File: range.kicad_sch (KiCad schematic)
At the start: 0 parts

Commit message: updated poer and range sensor scheamtics
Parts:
- added J2, J3, J4, J5, J6: Screw_Terminal_01x04, Connector_Dsub:DSUB-37_Pins_EdgeMount_P2.77mm, symbol Connector:Screw_Terminal_01x04
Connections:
- new net +3.3V: J2.1 (Pin_1), J3.1 (Pin_1), J4.1 (Pin_1), J5.1 (Pin_1), J6.1 (Pin_1)
- new net GND: J2.4 (Pin_4), J3.4 (Pin_4), J4.4 (Pin_4), J5.4 (Pin_4), J6.4 (Pin_4)
- new net SCL: J2.2 (Pin_2), J3.2 (Pin_2), J4.2 (Pin_2), J5.2 (Pin_2), J6.2 (Pin_2)
- new net SDA: J2.3 (Pin_3), J3.3 (Pin_3), J4.3 (Pin_3), J5.3 (Pin_3), J6.3 (Pin_3)
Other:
- note added: "Range Sensor Front"
- note added: "Range Sensor Front Left"
- note added: "Range Sensor Front Right"
- note added: "Range Sensor Left"
- note added: "Range Sensor Right"

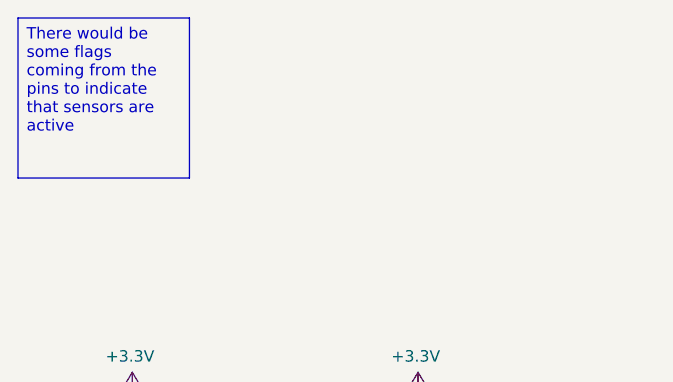
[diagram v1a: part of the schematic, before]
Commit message: added I2C lines
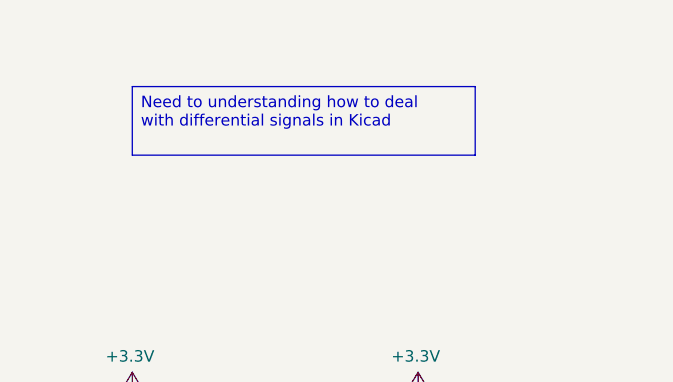
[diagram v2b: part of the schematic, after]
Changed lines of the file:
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@@
 		)
 	)
-	(text_box "There would be some flags coming from the pins to indicate that sensors are active "
+	(text_box "Need to understanding how to deal with differential signals in Kicad "
 		(exclude_from_sim no)
-		(at 20.32 16.51 0)
-		(size 19.05 17.78)
+		(at 33.02 24.13 0)
+		(size 38.1 7.62)
 		(margins 0.9525 0.9525 0.9525 0.9525)
 		(stroke

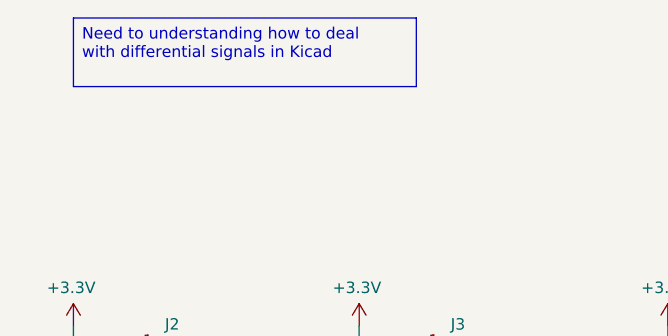
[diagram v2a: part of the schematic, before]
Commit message: added IR receiver circuit
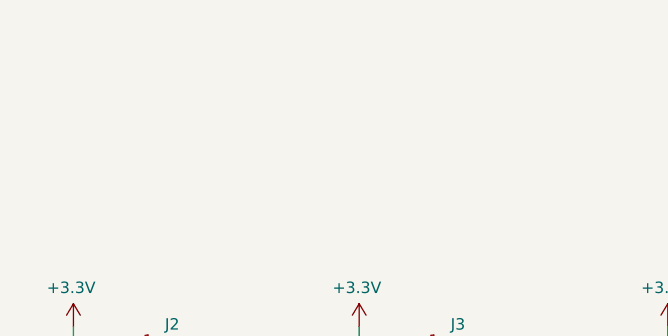
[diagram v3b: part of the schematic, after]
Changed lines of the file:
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@@
-		)
-	)
-	(text_box "Need to understanding how to deal with differential signals in Kicad "
-		(exclude_from_sim no)
-		(at 33.02 24.13 0)
-		(size 38.1 7.62)
-		(margins 0.9525 0.9525 0.9525 0.9525)
-		(stroke
-			(width 0)
-			(type solid)
-		)
-		(fill
-			(type none)
-		)
-		(effects
-			(font
-				(size 1.27 1.27)
-			)
-			(justify left top)
 		)
 	)

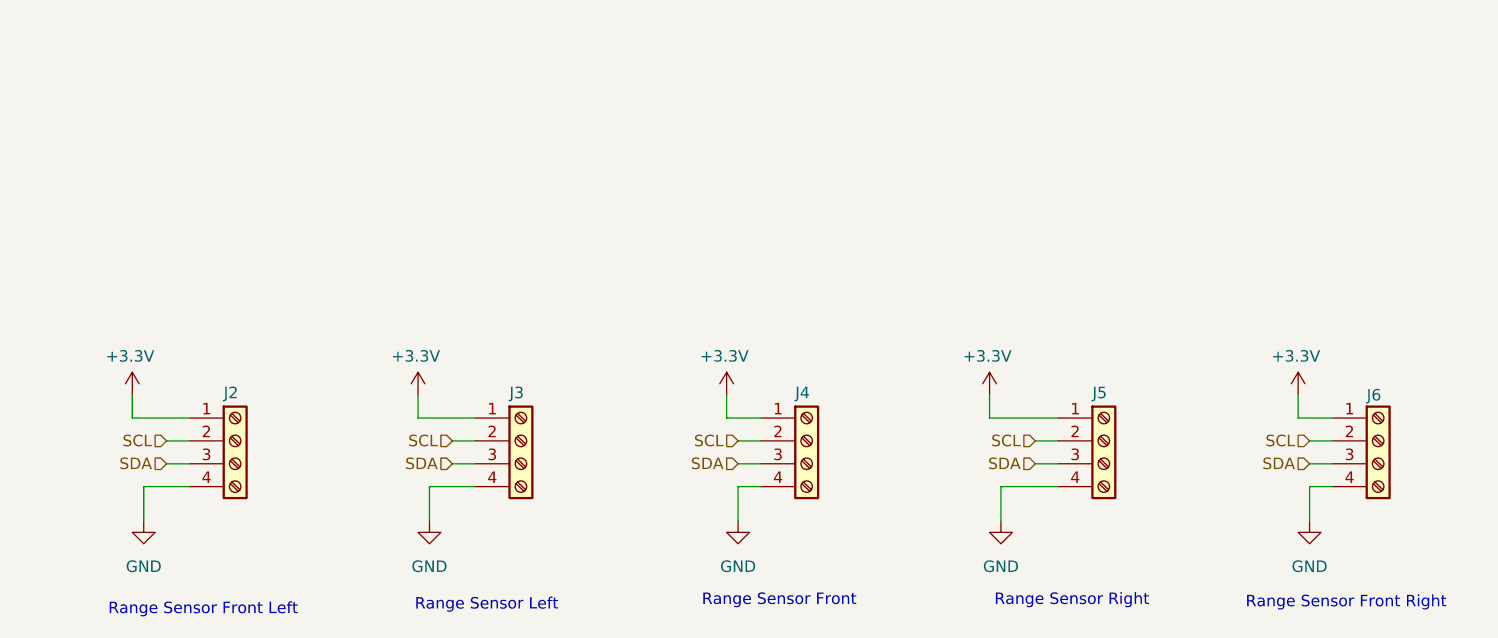
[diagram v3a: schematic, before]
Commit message: started adding DC Motor controller logic
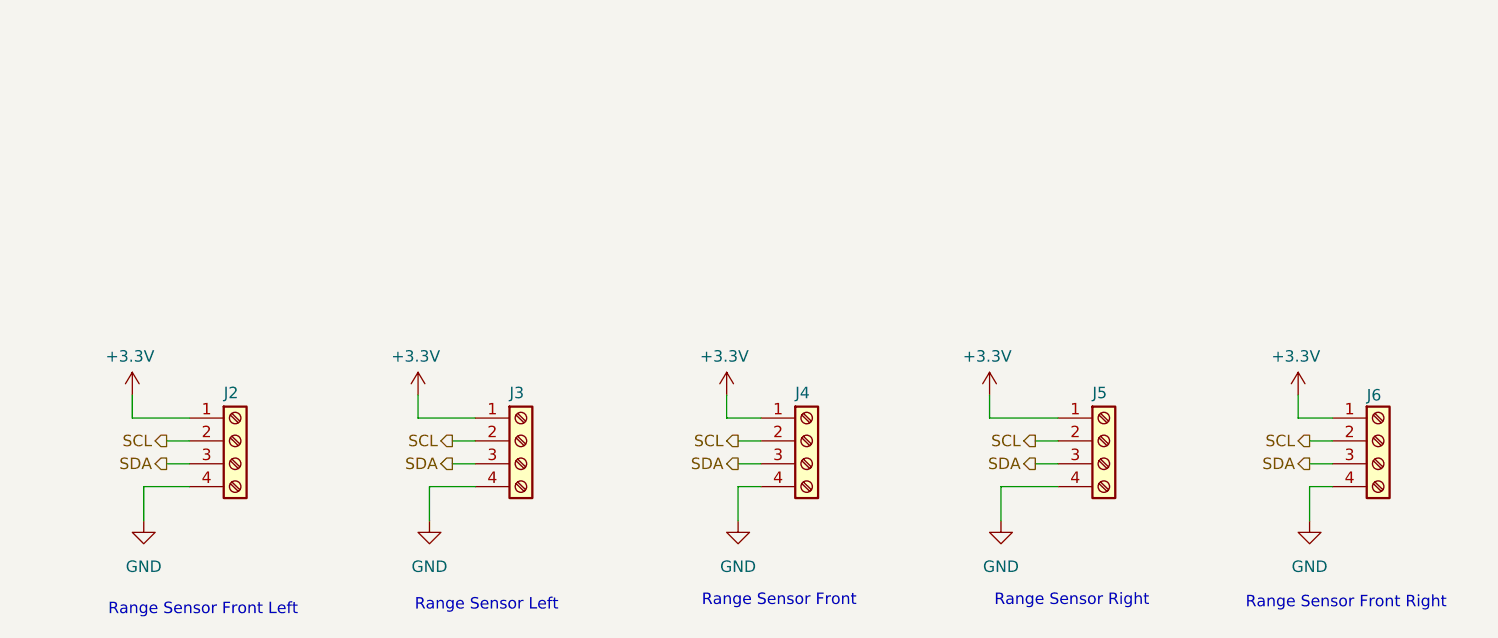
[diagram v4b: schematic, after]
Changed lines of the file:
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@@
 	)
 	(hierarchical_label "SDA"
-		(shape input)
+		(shape output)
 		(at 133.35 66.04 180)
 		(effects
@@
 	)
 	(hierarchical_label "SDA"
-		(shape input)
+		(shape output)
 		(at 68.58 66.04 180)
 		(effects
@@
 	)
 	(hierarchical_label "SDA"
-		(shape input)
+		(shape output)
 		(at 100.33 66.04 180)
 		(effects
@@
 	)
 	(hierarchical_label "SCL"
-		(shape input)
+		(shape output)
 		(at 133.35 63.5 180)
 		(effects
@@
 	)
 	(hierarchical_label "SCL"
-		(shape input)
+		(shape output)
 		(at 36.83 63.5 180)
 		(effects
@@
 	)
 	(hierarchical_label "SDA"
-		(shape input)
+		(shape output)
 		(at 163.83 66.04 180)
 		(effects
@@
 	)
 	(hierarchical_label "SCL"
-		(shape input)
+		(shape output)
 		(at 68.58 63.5 180)
 		(effects
@@
 	)
 	(hierarchical_label "SCL"
-		(shape input)
+		(shape output)
 		(at 100.33 63.5 180)
 		(effects
@@
 	)
 	(hierarchical_label "SDA"
-		(shape input)
+		(shape output)
 		(at 36.83 66.04 180)
 		(effects
@@
 	)
 	(hierarchical_label "SCL"
-		(shape input)
+		(shape output)
 		(at 163.83 63.5 180)
 		(effects

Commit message: started layout of Rev A
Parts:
- J2, J3, J4, J5, J6: footprint Connector_Dsub:DSUB-37_Pins_EdgeMount_P2.77mm -> TerminalBlock:TerminalBlock_Altech_AK300-4_P5.00mm
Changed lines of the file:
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@@
 			)
 		)
-		(property "Footprint" "Connector_Dsub:DSUB-37_Pins_EdgeMount_P2.77mm"
+		(property "Footprint" "TerminalBlock:TerminalBlock_Altech_AK300-4_P5.00mm"
 			(at 76.2 63.5 0)
 			(effects
@@
 			)
 		)
-		(property "Footprint" "Connector_Dsub:DSUB-37_Pins_EdgeMount_P2.77mm"
+		(property "Footprint" "TerminalBlock:TerminalBlock_Altech_AK300-4_P5.00mm"
 			(at 171.45 63.5 0)
 			(effects
@@
 			)
 		)
-		(property "Footprint" "Connector_Dsub:DSUB-37_Pins_EdgeMount_P2.77mm"
+		(property "Footprint" "TerminalBlock:TerminalBlock_Altech_AK300-4_P5.00mm"
 			(at 140.97 63.5 0)
 			(effects
@@
 			)
 		)
-		(property "Footprint" "Connector_Dsub:DSUB-37_Pins_EdgeMount_P2.77mm"
+		(property "Footprint" "TerminalBlock:TerminalBlock_Altech_AK300-4_P5.00mm"
 			(at 107.95 63.5 0)
 			(effects
@@
 			)
 		)
-		(property "Footprint" "Connector_Dsub:DSUB-37_Pins_EdgeMount_P2.77mm"
+		(property "Footprint" "TerminalBlock:TerminalBlock_Altech_AK300-4_P5.00mm"
 			(at 44.45 63.5 0)
 			(effects

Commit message: added all footprints and step files to components
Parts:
- J2, J3, J4, J5, J6: footprint TerminalBlock:TerminalBlock_Altech_AK300-4_P5.00mm -> TerminalBlock_Phoenix:TerminalBlock_Phoenix_MKDS-1,5-4_1x04_P5.00mm_Horizontal
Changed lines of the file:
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@@
 			)
 		)
-		(property "Footprint" "TerminalBlock:TerminalBlock_Altech_AK300-4_P5.00mm"
+		(property "Footprint" "TerminalBlock_Phoenix:TerminalBlock_Phoenix_MKDS-1,5-4_1x04_P5.00mm_Horizontal"
 			(at 76.2 63.5 0)
 			(effects
@@
 			)
 		)
-		(property "Footprint" "TerminalBlock:TerminalBlock_Altech_AK300-4_P5.00mm"
+		(property "Footprint" "TerminalBlock_Phoenix:TerminalBlock_Phoenix_MKDS-1,5-4_1x04_P5.00mm_Horizontal"
 			(at 171.45 63.5 0)
 			(effects
@@
 			)
 		)
-		(property "Footprint" "TerminalBlock:TerminalBlock_Altech_AK300-4_P5.00mm"
+		(property "Footprint" "TerminalBlock_Phoenix:TerminalBlock_Phoenix_MKDS-1,5-4_1x04_P5.00mm_Horizontal"
 			(at 140.97 63.5 0)
 			(effects
@@
 			)
 		)
-		(property "Footprint" "TerminalBlock:TerminalBlock_Altech_AK300-4_P5.00mm"
+		(property "Footprint" "TerminalBlock_Phoenix:TerminalBlock_Phoenix_MKDS-1,5-4_1x04_P5.00mm_Horizontal"
 			(at 107.95 63.5 0)
 			(effects
@@
 			)
 		)
-		(property "Footprint" "TerminalBlock:TerminalBlock_Altech_AK300-4_P5.00mm"
+		(property "Footprint" "TerminalBlock_Phoenix:TerminalBlock_Phoenix_MKDS-1,5-4_1x04_P5.00mm_Horizontal"
 			(at 44.45 63.5 0)
 			(effects

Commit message: updated infomration on schematic; started working on layout
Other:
- company: (none) -> Erick Zamora 
- title: (none) -> Miniature Sumo Robot 
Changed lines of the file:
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@@
 	(generator_version "9.0")
 	(paper "A5")
+	(title_block
+		(title "Miniature Sumo Robot ")
+		(date "2025-09-26")
+		(rev "A")
+		(company "Erick Zamora ")
+	)
 	(text "Range Sensor Left\n"
 		(exclude_from_sim no)
